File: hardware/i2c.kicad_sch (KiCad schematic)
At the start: 21 parts, among them Q2 SS8550, Q3 SS8050, U11 SAINTCON-Minibadge, U12 SAINTCON-Minibadge, U3 SAINTCON-Minibadge, U4 SAINTCON-Minibadge, U5 SAINTCON-Minibadge, U6 SAINTCON-Minibadge, U8 SAINTCON-Minibadge, U9 SAINTCON-Minibadge

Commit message: accel added
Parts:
- added C23: 1uF, C_0603_1608Metric, symbol Device:C_US
- added C24: 100nF, C_0603_1608Metric, symbol Device:C_US
- added U13: STK8321, Package_LGA:LGA-12_2x2mm_P0.5mm, symbol Sensor_Motion:KX022-1020
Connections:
- net +3.3V: now also C23.1, C24.1, U13.10 (~{CS}), U13.3 (IO_VDD), U13.7 (VDD)
- net GND: now also C23.2, C24.2, U13.4 (TRIG), U13.8 (GNDIO), U13.9 (GND)
- net SCL: now also U13.12 (SCLK/SCL)
- net SDA: now also U13.2 (SDI/SDA)
- no-connect marks 33 -> 37

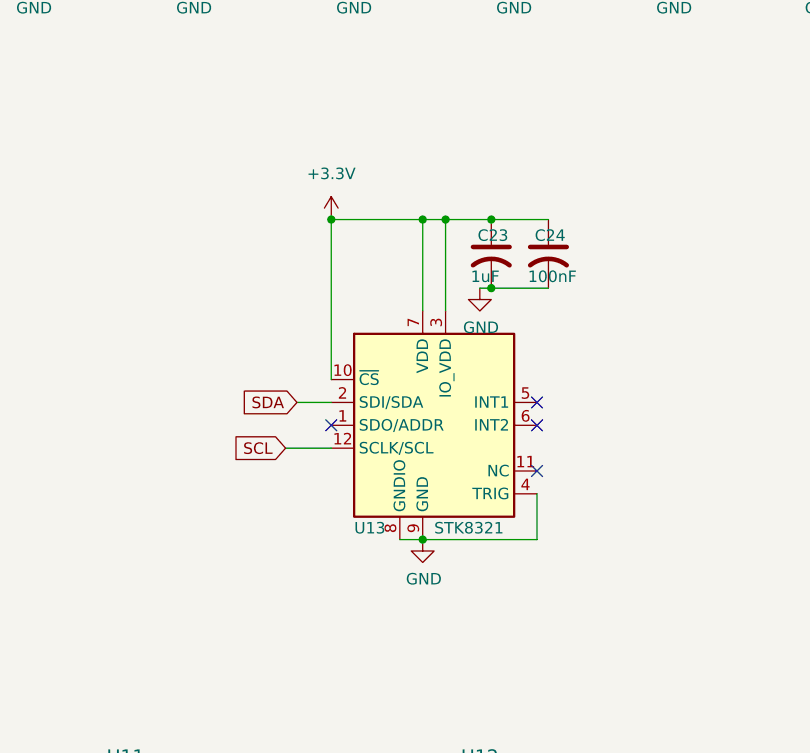
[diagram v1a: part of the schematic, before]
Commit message: Restoring Orion trail
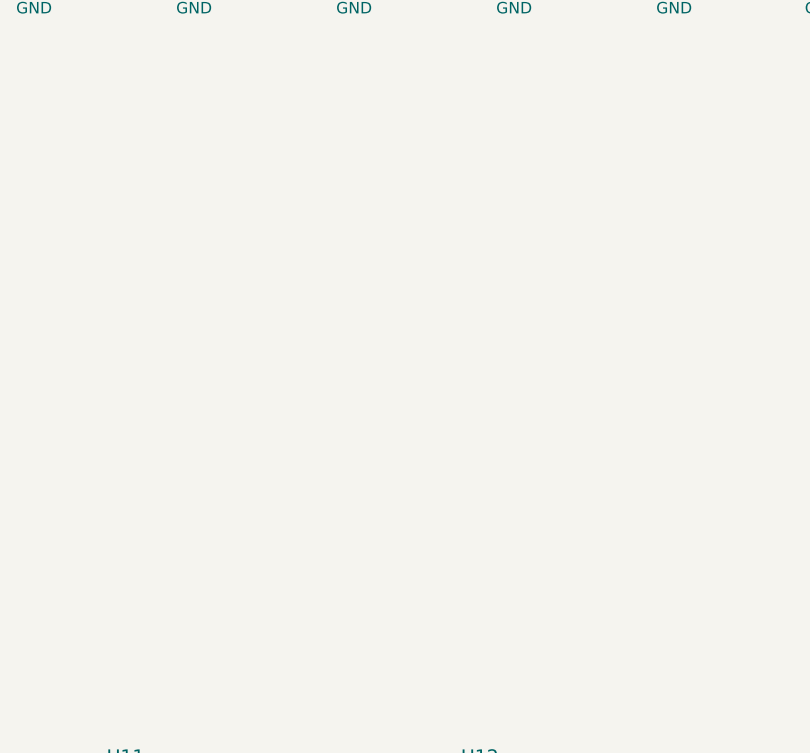
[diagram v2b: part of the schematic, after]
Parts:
- removed C23: 1uF, C_0603_1608Metric, symbol Device:C_US
- removed C24: 100nF, C_0603_1608Metric, symbol Device:C_US
- removed U13: STK8321, Package_LGA:LGA-12_2x2mm_P0.5mm, symbol Sensor_Motion:KX022-1020
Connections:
- no-connect marks 37 -> 33
